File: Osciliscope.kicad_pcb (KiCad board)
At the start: 2 copper layers, 39.6 x 60.2 mm, 42 parts, among them J1 U.FL, J2 Conn_01x04_Socket, J3 U.FL, J4 Conn_01x04_Socket, J5 USB_C_Receptacle_USB2.0_14P, J6 Conn_01x02_MountingPin, SW1 SW_Rotary_1x8_MP, SW2 SW_Rotary_1x8_MP, SW3 SW_Nidec_CAS-120A1, SW4 SW_Nidec_CAS-120A1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

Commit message: pcb update
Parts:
- removed SW1, SW2: SW_Rotary_1x8_MP, Rotary_Encoder:RotaryEncoder_Alps_EC11E-Switch_Vertical_H20mm_CircularMountingHoles
- moved J3 17.6 mm to (80.5, 181.0)
- moved C11 12.9 mm to (104.8, 153.7)
- moved C2 12.9 mm to (77.8, 155.9)
- moved C3 12.9 mm to (108.2, 161.4)
- moved C4 12.9 mm to (99.8, 165.3)
- moved C5 12.9 mm to (94.3, 165.3)
- moved D1 12.9 mm to (111.8, 161.4)
- moved D3 12.9 mm to (82.1, 162.6)
- moved D4 12.9 mm to (79.8, 162.6)
- moved D5 12.9 mm to (79.3, 144.3)
- moved J4 12.9 mm to (94.2, 152.6)
- moved J6 12.9 mm to (77.5, 148.3)
- moved R10 12.9 mm to (108.7, 169.4)
- moved R12 12.9 mm to (93.5, 162.9)
- moved R3 12.9 mm to (112.8, 159.3)
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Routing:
- removed copper zone on F.Cu, net GND
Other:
- board size 39.6 x 60.2 mm -> 51 x 102 mm

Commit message: PCB Fixed
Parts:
- removed J1: U.FL, Connector_Coaxial:BNC_Amphenol_031-5539_Vertical
- added C14: 1uF, Capacitor_SMD:C_1206_3216Metric, F.Cu at (104.1, 123.0)
- added C15: 1uF, Capacitor_SMD:C_1206_3216Metric, F.Cu at (104.1, 126.4)
- added C16: 1uF, Capacitor_SMD:C_1206_3216Metric, F.Cu at (104.1, 129.8)
- added C17: 1uF, Capacitor_SMD:C_1206_3216Metric, F.Cu at (104.1, 133.1)
- added C18: 1uF, Capacitor_SMD:C_1206_3216Metric, F.Cu at (104.1, 136.4)
- added C19: 1uF, Capacitor_SMD:C_1206_3216Metric, F.Cu at (104.1, 139.8)
- added J7: U.FL, Connector_Coaxial:BNC_Amphenol_031-5539_Vertical, F.Cu at (110.8, 180.8)
- added R1: 10k, Capacitor_SMD:C_0603_1608Metric, F.Cu at (108.9, 122.6)
- added R15: 10k, Capacitor_SMD:C_0603_1608Metric, F.Cu at (112.9, 127.7)
- added R16: 10k, Capacitor_SMD:C_0603_1608Metric, F.Cu at (112.9, 130.2)
- added R17: 10k, Capacitor_SMD:C_0603_1608Metric, F.Cu at (98.2, 133.1)
- added R18: 1M, Capacitor_SMD:C_0603_1608Metric, F.Cu at (82.2, 171.4)
- added R19: 1M, Capacitor_SMD:C_0603_1608Metric, F.Cu at (111.8, 170.4)
- added R2: 10k, Capacitor_SMD:C_0603_1608Metric, F.Cu at (108.9, 125.1)
- added R20: 100k, Capacitor_SMD:C_0603_1608Metric, F.Cu at (116.2, 170.4)
- added R5: 10k, Capacitor_SMD:C_0603_1608Metric, F.Cu at (108.9, 127.7)
- added R6: 10k, Capacitor_SMD:C_0603_1608Metric, F.Cu at (108.9, 130.2)
- added R7: 10k, Capacitor_SMD:C_0603_1608Metric, F.Cu at (108.9, 132.7)
- added R8: 10k, Capacitor_SMD:C_0603_1608Metric, F.Cu at (112.9, 122.6)
- added R9: 10k, Capacitor_SMD:C_0603_1608Metric, F.Cu at (112.9, 125.1)
- added SW1: RotaryEncoder_Switch, Rotary_Encoder:RotaryEncoder_Alps_EC11E-Switch_Vertical_H20mm, F.Cu at (78.1, 116.5)
- added SW5: RotaryEncoder_Switch, Rotary_Encoder:RotaryEncoder_Alps_EC11E-Switch_Vertical_H20mm, F.Cu at (97.7, 116.2)
- added SW6: RotaryEncoder_Switch, Rotary_Encoder:RotaryEncoder_Alps_EC11E-Switch_Vertical_H20mm, F.Cu at (78.1, 136.2)
- C10, C9: value 1u -> 1uF
- R14: value 1M -> 100k
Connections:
- C10 pad 1: Net-(J3-In) -> Net-(SW4-A)
- C9 pad 1: Net-(J1-In) -> Net-(SW3-A)
- R14 pad 1: Net-(J3-In) -> Net-(SW4-A)
- R3 pad 2: Net-(D1-A) -> unconnected-(R3-Pad2)
- R4 pad 2: Net-(D3-A) -> Net-(SW4-B)
- SW3 pad 2: Net-(D1-A) -> unconnected-(SW3-B-Pad2)
- SW3 pad 3: Net-(J1-In) -> Net-(SW3-A)
- SW4 pad 2: Net-(D3-A) -> Net-(SW4-B)
- SW4 pad 3: Net-(J3-In) -> Net-(SW4-A)
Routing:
- net Net-(SW4-A): track 0.00 -> 20.9 mm
- net Net-(J7-In): track 0.00 -> 10.0 mm
- net Net-(J1-In): track 16.7 -> 6.75 mm
- net Net-(SW3-A): track 0.00 -> 7.24 mm
- net Net-(J3-In): track 17.7 -> 10.6 mm
- added copper zone on F.Cu, net GND

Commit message: Changes
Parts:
- removed R10: 1M, Capacitor_SMD:C_0603_1608Metric
- added J1: Conn_01x09_Socket, Connector_PinHeader_2.00mm:PinHeader_1x09_P2.00mm_Vertical, F.Cu at (75.0, 113.8)
- moved C15 24.9 mm to (96.2, 102.8)
- moved R5 23.5 mm to (94.8, 108.8), turned to 90 degrees
- moved C14 19.1 mm to (96.2, 105.6)
- moved R2 19.1 mm to (94.8, 112.2), turned to -90 degrees
- moved C17 18.3 mm to (111.2, 116.2)
- moved R9 18.0 mm to (95.0, 123.8), turned to 90 degrees
- moved R15 16.4 mm to (97.0, 123.8), turned to 90 degrees
- moved R1 16.1 mm to (96.6, 112.2), turned to -90 degrees
- moved R16 16.0 mm to (97.2, 127.4), turned to -90 degrees
- moved R7 14.4 mm to (112.8, 118.8)
- moved C16 13.5 mm to (105.2, 116.2), turned to 180 degrees
- moved R6 12.3 mm to (104.6, 118.7)
- moved SW5 10.3 mm to (107.5, 113.1)
- moved C19 10.1 mm to (96.4, 133.2)
- moved C18 9.65 mm to (96.4, 130.6)
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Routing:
- net V3.3: track 81.5 -> 163.7 mm, vias 4 -> 7
- net H_dt: track 0.00 -> 50.7 mm, vias 0 -> 1
- net H_clk: track 0.00 -> 44.6 mm
- net Trig_dt: track 0.00 -> 42.6 mm
- net V_dt: track 0.00 -> 39.6 mm
- net Trig_clk: track 0.00 -> 38.2 mm, vias 0 -> 1
- net Ch2_vis: track 0.00 -> 33.8 mm
- net V_clk: track 0.00 -> 31.9 mm
- net Net-(R7-Pad2): track 0.00 -> 21.7 mm
- net GND: track 27.7 -> 45.2 mm, vias 12 -> 17
- net Net-(R2-Pad2): track 0.00 -> 17.0 mm, vias 0 -> 2
- net Trig_ch: track 0.00 -> 16.6 mm
- net USBCRAW: track 36.8 -> 51.3 mm
- net Net-(D3-A): track 13.2 -> 1.66 mm
- net Net-(SW4-B): track 0.00 -> 10.9 mm
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
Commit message: DOUBLE POWAH
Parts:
- removed D2, D3, D4: D, Diode_SMD:D_0201_0603Metric
- removed J6: Conn_01x02_MountingPin, Connector_PinHeader_2.00mm:PinHeader_1x02_P2.00mm_Vertical
- removed U3: IP2721, Package_SO:TSSOP-16_4.4x5mm_P0.65mm
- removed U8: MCP4251-104E/ML-ND, Package_SO:TSSOP-14-1EP_4.4x5mm_P0.65mm
- added C20: 20pF, Capacitor_SMD:C_1206_3216Metric, F.Cu at (145.8, 99.6)
- added J8: USB_C_Receptacle_USB2.0_14P, Connector_USB:USB_C_Receptacle_Amphenol_124019772112A, F.Cu at (161.0, 95.3)
- added R10: 10k, Capacitor_SMD:C_0603_1608Metric, F.Cu at (116.0, 96.3)
- added R14: 1M, Capacitor_SMD:C_0603_1608Metric, F.Cu at (116.0, 98.8)
- added R18: 10k, Capacitor_SMD:C_0603_1608Metric, F.Cu at (116.0, 101.3)
- added R19: 1M, Capacitor_SMD:C_0603_1608Metric, F.Cu at (116.0, 103.8)
- added R20: 1M, Capacitor_SMD:C_0603_1608Metric, F.Cu at (116.0, 106.3)
- added R21: 1M, Capacitor_SMD:C_0603_1608Metric, F.Cu at (116.0, 108.8)
- C11: value 1uF -> 100n
- C12: value 10u -> 100n
- D1: value D -> 1N4001; footprint Diode_SMD:D_0201_0603Metric -> Diode_THT:D_DO-41_SOD81_P10.16mm_Horizontal
- R14, R20: value 100k -> 1M
- R18: value 1M -> 10k
- R3, R4: value 5k -> 10k
- U4: value AZ1084-5.0 -> CH340N; footprint Package_TO_SOT_SMD:TO-252-2 -> Package_SO:JEITA_SOIC-8_3.9x4.9mm_P1.27mm
- moved U4 73.9 mm to (152.0, 108.6), turned to -90 degrees
- moved D1 72.6 mm to (152.0, 101.0), turned to 90 degrees
- moved C11 60.9 mm to (146.0, 108.9)
- moved J2 59.6 mm to (138.8, 134.2)
- moved C2 59.6 mm to (119.9, 113.8)
- moved C3 59.6 mm to (150.4, 119.3)
- moved C4 59.6 mm to (141.9, 123.2)
- moved C5 59.6 mm to (136.5, 123.2)
- moved D5 59.6 mm to (121.5, 102.2)
- moved R1 59.6 mm to (138.8, 70.1)
- moved R17 59.6 mm to (137.2, 85.3)
- moved R3 59.6 mm to (154.9, 117.2)
- moved R6 59.6 mm to (146.8, 76.5)
- moved J7 59.6 mm to (152.9, 138.7)
- moved R19 59.6 mm to (153.9, 128.3)
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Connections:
- net C2_G_IN renamed Net-(U7--)
- net C2_G_OUT renamed CHAN_2
- C10 pad 1: Net-(SW4-A) -> Net-(J3-In)
- C11 pad 1: USBCRAW -> 5Vin
- C12 pad 1: USBCRAW -> Net-(U4-V3)
- C9 pad 1: Net-(SW3-A) -> Net-(J7-In)
- D1 pad 1: V3.3 -> 5Vin
- J5 pad A4: USBCRAW -> 5Vin
- J5 pad A6: unconnected-(J5-D+-PadA6) -> Net-(U4-UD+)
- J5 pad A7: unconnected-(J5-D--PadA7) -> Net-(U4-UD-)
- J5 pad A9: USBCRAW -> 5Vin
- J5 pad B4: USBCRAW -> 5Vin
- J5 pad B6: unconnected-(J5-D+-PadB6) -> Net-(U4-UD+)
- J5 pad B7: unconnected-(J5-D--PadB7) -> Net-(U4-UD-)
- J5 pad B9: USBCRAW -> 5Vin
- R14 pad 1: Net-(SW4-A) -> GND
- R14 pad 2: GND -> Net-(J3-In)
- R18 pad 1: Net-(SW4-A) -> CHAN_1
- R18 pad 2: Net-(J3-In) -> Net-(U5--)
- R19 pad 1: Net-(SW3-A) -> Net-(J7-In)
- R19 pad 2: Net-(J7-In) -> Net-(SW3-C)
- R20 pad 1: Net-(SW3-A) -> GND
- R20 pad 2: GND -> Net-(J7-In)
- R3 pad 1: C1_G_IN -> Net-(U5--)
- R3 pad 2: unconnected-(R3-Pad2) -> Net-(SW3-B)
- SW3 pad 2: unconnected-(SW3-B-Pad2) -> Net-(SW3-B)
- SW3 pad 3: Net-(SW3-A) -> Net-(J7-In)
- SW4 pad 3: Net-(SW4-A) -> Net-(J3-In)
- U2 pad 5: C1_G_OUT -> CHAN_1
- U4 pad 1: GND -> Net-(U4-UD+)
- U4 pad 2: 5Vin -> Net-(U4-UD-)
- U4 pad 3: USBCRAW -> GND
- U5 pad 1: C1_G_OUT -> CHAN_1
- U5 pad 4: C1_G_IN -> Net-(U5--)
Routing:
- net V3.3: track 163.7 -> 96.4 mm
- net USBCRAW: track 51.3 -> 0.00 mm
- net 5Vin: track 22.5 -> 47.3 mm
- net C1_G_IN: track 19.2 -> 0.00 mm, vias 2 -> 0
- net C1_G_OUT: track 18.2 -> 0.00 mm, vias 2 -> 0
- net Net-(J5-CC2): track 17.7 -> 0.00 mm, vias 2 -> 0
- net RPI_DIN_DP: track 17.3 -> 0.00 mm, vias 2 -> 0
- net Net-(U5--): track 0.00 -> 15.8 mm, vias 0 -> 2
- net Net-(J5-CC1): track 13.3 -> 0.00 mm
- net RPI_SCLK_DP: track 12.4 -> 0.00 mm, vias 2 -> 0
- net Net-(SW3-A): track 11.4 -> 0.00 mm
- net CHAN_2: track 18.6 -> 7.44 mm, vias 2 -> 0
- net Net-(SW4-A): track 10.9 -> 0.00 mm
- net Net-(D1-A): track 2.52 -> 13.4 mm
- net Net-(J3-In): track 10.6 -> 0.00 mm
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
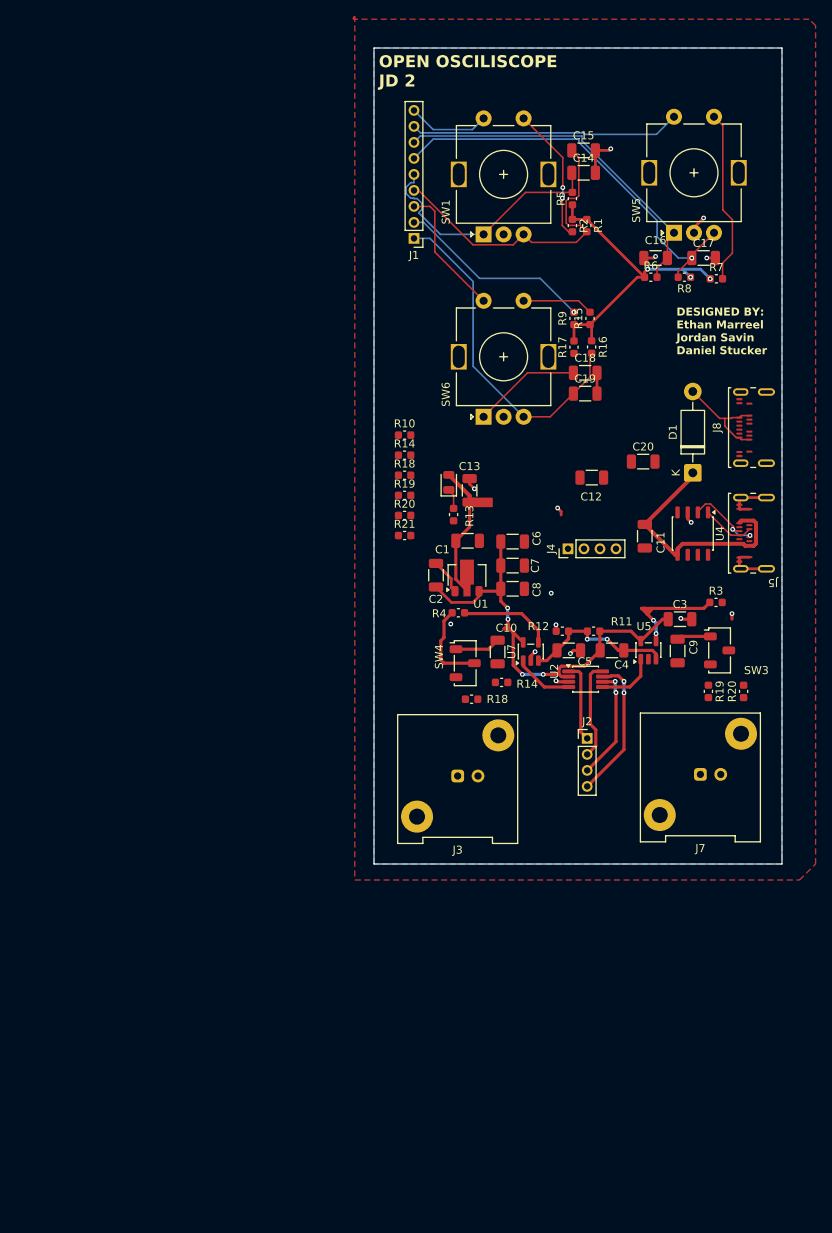
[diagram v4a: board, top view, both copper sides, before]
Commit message: Revert "DOUBLE POWAH"
This reverts commit d7c18ef275ed38aaaeedcd9803d9307ce1c33910.
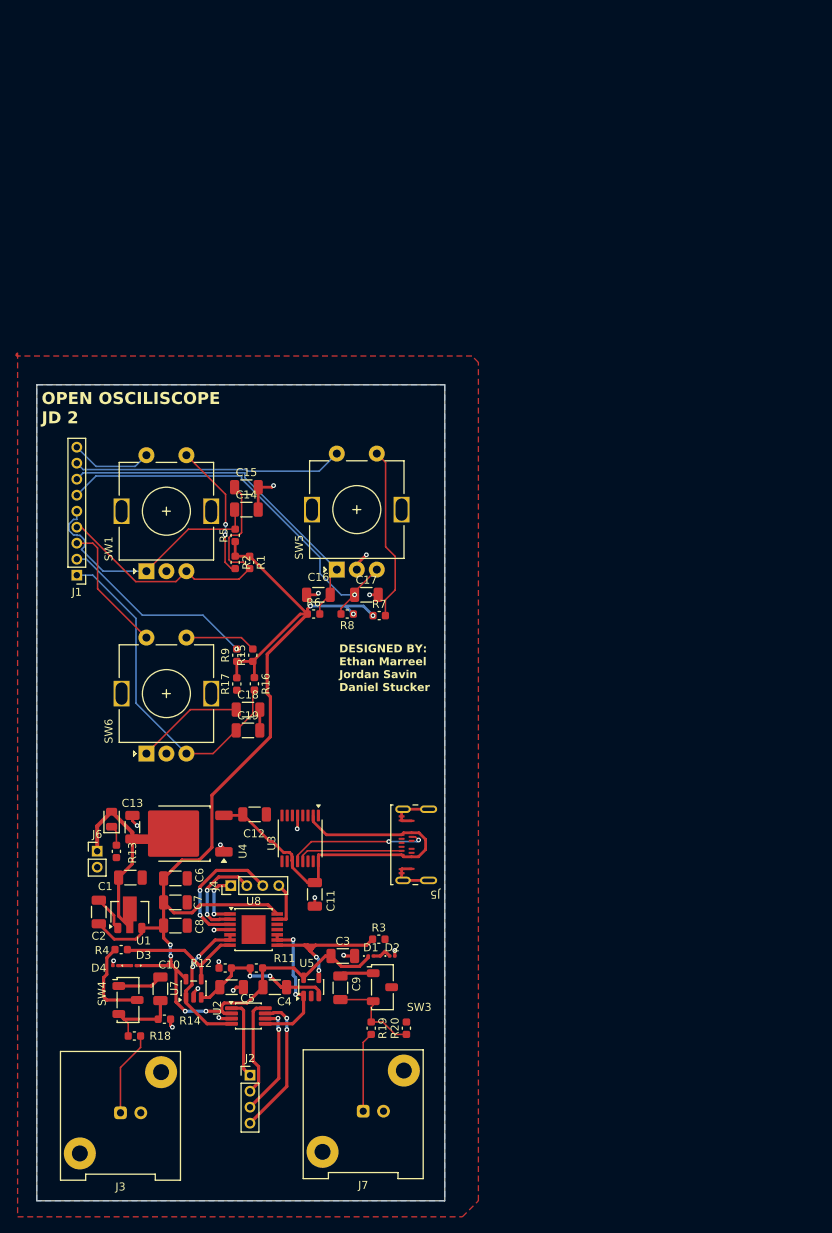
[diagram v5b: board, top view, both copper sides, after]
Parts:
- removed C20: 20pF, Capacitor_SMD:C_1206_3216Metric
- removed J8: USB_C_Receptacle_USB2.0_14P, Connector_USB:USB_C_Receptacle_Amphenol_124019772112A
- removed R10: 10k, Capacitor_SMD:C_0603_1608Metric
- removed the R14 at (116.0, 98.8)
- removed the R18 at (116.0, 101.3)
- removed the R19 at (116.0, 103.8)
- removed the R20 at (116.0, 106.3)
- removed R21: 1M, Capacitor_SMD:C_0603_1608Metric
- added D2: D, Diode_SMD:D_0201_0603Metric, F.Cu at (114.4, 161.4)
- added D3: D, Diode_SMD:D_0201_0603Metric, F.Cu at (82.1, 162.6)
- added D4: D, Diode_SMD:D_0201_0603Metric, F.Cu at (79.8, 162.6)
- added J6: Conn_01x02_MountingPin, Connector_PinHeader_2.00mm:PinHeader_1x02_P2.00mm_Vertical, F.Cu at (77.5, 148.3)
- added U3: IP2721, Package_SO:TSSOP-16_4.4x5mm_P0.65mm, F.Cu at (102.9, 146.7)
- added U8: MCP4251-104E/ML-ND, Package_SO:TSSOP-14-1EP_4.4x5mm_P0.65mm, F.Cu at (97.1, 158.1)
- C11: value 100n -> 1uF
- C12: value 100n -> 10u
- D1: value 1N4001 -> D; footprint Diode_THT:D_DO-41_SOD81_P10.16mm_Horizontal -> Diode_SMD:D_0201_0603Metric
- R14, R20: value 1M -> 100k
- R18: value 10k -> 1M
- R3, R4: value 10k -> 5k
- U4: value CH340N -> AZ1084-5.0; footprint Package_SO:JEITA_SOIC-8_3.9x4.9mm_P1.27mm -> Package_TO_SOT_SMD:TO-252-2
- moved U4 73.9 mm to (88.3, 146.1), turned to 180 degrees
- moved D1 72.6 mm to (111.8, 161.4), turned to 0 degrees
- moved C11 60.9 mm to (104.8, 153.7)
- moved J2 59.6 mm to (96.7, 176.3)
- moved C2 59.6 mm to (77.8, 155.9)
- moved C3 59.6 mm to (108.2, 161.4)
- moved C4 59.6 mm to (99.8, 165.3)
- moved C5 59.6 mm to (94.3, 165.3)
- moved D5 59.6 mm to (79.3, 144.3)
- moved R1 59.6 mm to (96.6, 112.2)
- moved R17 59.6 mm to (95.0, 127.4)
- moved R3 59.6 mm to (112.8, 159.3)
- moved R6 59.6 mm to (104.6, 118.7)
- moved J7 59.6 mm to (110.8, 180.8)
- moved R19 59.6 mm to (111.8, 170.4)
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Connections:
- net CHAN_2 renamed C2_G_OUT
- net Net-(U7--) renamed C2_G_IN
- C10 pad 1: Net-(J3-In) -> Net-(SW4-A)
- C11 pad 1: 5Vin -> USBCRAW
- C12 pad 1: Net-(U4-V3) -> USBCRAW
- C9 pad 1: Net-(J7-In) -> Net-(SW3-A)
- D1 pad 1: 5Vin -> V3.3
- J5 pad A4: 5Vin -> USBCRAW
- J5 pad A6: Net-(U4-UD+) -> unconnected-(J5-D+-PadA6)
- J5 pad A7: Net-(U4-UD-) -> unconnected-(J5-D--PadA7)
- J5 pad A9: 5Vin -> USBCRAW
- J5 pad B4: 5Vin -> USBCRAW
- J5 pad B6: Net-(U4-UD+) -> unconnected-(J5-D+-PadB6)
- J5 pad B7: Net-(U4-UD-) -> unconnected-(J5-D--PadB7)
- J5 pad B9: 5Vin -> USBCRAW
- R14 pad 1: GND -> Net-(SW4-A)
- R14 pad 2: Net-(J3-In) -> GND
- R18 pad 1: CHAN_1 -> Net-(SW4-A)
- R18 pad 2: Net-(U5--) -> Net-(J3-In)
- R19 pad 1: Net-(J7-In) -> Net-(SW3-A)
- R19 pad 2: Net-(SW3-C) -> Net-(J7-In)
- R20 pad 1: GND -> Net-(SW3-A)
- R20 pad 2: Net-(J7-In) -> GND
- R3 pad 1: Net-(U5--) -> C1_G_IN
- R3 pad 2: Net-(SW3-B) -> unconnected-(R3-Pad2)
- SW3 pad 2: Net-(SW3-B) -> unconnected-(SW3-B-Pad2)
- SW3 pad 3: Net-(J7-In) -> Net-(SW3-A)
- SW4 pad 3: Net-(J3-In) -> Net-(SW4-A)
- U2 pad 5: CHAN_1 -> C1_G_OUT
- U4 pad 1: Net-(U4-UD+) -> GND
- U4 pad 2: Net-(U4-UD-) -> 5Vin
- U4 pad 3: GND -> USBCRAW
- U5 pad 1: CHAN_1 -> C1_G_OUT
- U5 pad 4: Net-(U5--) -> C1_G_IN
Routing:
- net V3.3: track 96.4 -> 163.7 mm
- net USBCRAW: track 0.00 -> 51.3 mm
- net 5Vin: track 47.3 -> 22.5 mm
- net C1_G_IN: track 0.00 -> 19.2 mm, vias 0 -> 2
- net C1_G_OUT: track 0.00 -> 18.2 mm, vias 0 -> 2
- net Net-(J5-CC2): track 0.00 -> 17.7 mm, vias 0 -> 2
- net RPI_DIN_DP: track 0.00 -> 17.3 mm, vias 0 -> 2
- net Net-(U5--): track 15.8 -> 0.00 mm, vias 2 -> 0
- net Net-(J5-CC1): track 0.00 -> 13.3 mm
- net RPI_SCLK_DP: track 0.00 -> 12.4 mm, vias 0 -> 2
- net Net-(SW3-A): track 0.00 -> 11.4 mm
- net C2_G_OUT: track 7.44 -> 18.6 mm, vias 0 -> 2
- net Net-(SW4-A): track 0.00 -> 10.9 mm
- net Net-(D1-A): track 13.4 -> 2.52 mm
- net Net-(J3-In): track 0.00 -> 10.6 mm
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
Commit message: DOUBLE POWAH
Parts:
- removed C11: 1uF, Capacitor_SMD:C_1206_3216Metric
- removed C12, C13: 10u, Capacitor_SMD:C_1206_3216Metric
- removed D1, D2, D3, D4: D, Diode_SMD:D_0201_0603Metric
- removed J4: Conn_01x04_Socket, Connector_PinHeader_2.00mm:PinHeader_1x04_P2.00mm_Vertical
- removed SW3: SW_Nidec_CAS-120A1, Button_Switch_SMD:Nidec_Copal_CAS-120A
- removed U4: AZ1084-5.0, Package_TO_SOT_SMD:TO-252-2
- removed U8: MCP4251-104E/ML-ND, Package_SO:TSSOP-14-1EP_4.4x5mm_P0.65mm
- added C20: 20pF, Capacitor_SMD:C_1206_3216Metric, F.Cu at (87.0, 168.4)
- added C21: 20pF, Capacitor_SMD:C_1206_3216Metric, F.Cu at (114.0, 170.8)
- added J8: USB_C_Receptacle_USB2.0_14P, Connector_USB:USB_C_Receptacle_Amphenol_124019772112A, F.Cu at (119.0, 159.9)
- added J9: Conn_01x03_Socket, Connector_PinSocket_2.00mm:PinSocket_1x03_P2.00mm_Vertical, F.Cu at (110.2, 153.6)
- added R10: 5k, Capacitor_SMD:C_0603_1608Metric, F.Cu at (80.6, 159.8)
- added R21: 5.5k, Capacitor_SMD:C_0603_1608Metric, F.Cu at (116.0, 167.0)
- added R22: 5.5k, Capacitor_SMD:C_0603_1608Metric, F.Cu at (111.8, 147.8)
- added R23: 5.5k, Capacitor_SMD:C_0603_1608Metric, F.Cu at (111.8, 144.5)
- added SW7: SW_Nidec_CAS-120A1, Button_Switch_SMD:Nidec_Copal_CAS-120A, F.Cu at (104.2, 166.4)
- added TP1: TestPoint, TestPoint:TestPoint_Pad_3.0x3.0mm, F.Cu at (118.8, 170.8)
- added TP2: TestPoint, TestPoint:TestPoint_Pad_3.0x3.0mm, F.Cu at (77.0, 161.2)
- added TP3: TestPoint, TestPoint:TestPoint_Pad_3.0x3.0mm, F.Cu at (92.0, 168.2)
- added TP4: TestPoint, TestPoint:TestPoint_Pad_3.0x3.0mm, F.Cu at (90.6, 163.2)
- added TP5: TestPoint, TestPoint:TestPoint_Pad_3.0x3.0mm, F.Cu at (77.0, 151.6)
- added TP6: TestPoint, TestPoint:TestPoint_Pad_3.0x3.0mm, F.Cu at (77.0, 156.2)
- added U6: TLV9061xDBV, Package_TO_SOT_SMD:SOT-23-5, F.Cu at (86.2, 151.4)
- J1: footprint Connector_PinHeader_2.00mm:PinHeader_1x09_P2.00mm_Vertical -> Connector_PinSocket_2.00mm:PinSocket_1x09_P2.00mm_Vertical
- J6: footprint Connector_PinHeader_2.00mm:PinHeader_1x02_P2.00mm_Vertical -> Connector_PinSocket_2.00mm:PinSocket_1x02_P2.00mm_Vertical
- R14, R20: value 100k -> 1M
- R18: value 1M -> 5k
- R19: value 1M -> 5.5k
- U3: value IP2721 -> CH340N; footprint Package_SO:TSSOP-16_4.4x5mm_P0.65mm -> Package_SO:JEITA_SOIC-8_3.9x4.9mm_P1.27mm
- moved J6 40.0 mm to (116.6, 139.8), turned to 90 degrees
- moved U1 26.6 mm to (107.4, 149.4), turned to 0 degrees
- moved C1 26.5 mm to (107.0, 143.6)
- moved C2 25.0 mm to (101.8, 149.2)
- moved C4 24.3 mm to (81.0, 149.8), turned to -90 degrees
- moved R18 23.5 mm to (104.0, 162.6), turned to 180 degrees
- moved R13 22.5 mm to (101.2, 141.0), turned to 180 degrees
- moved D5 22.1 mm to (101.4, 144.6), turned to 0 degrees
- moved C5 17.1 mm to (81.0, 154.6), turned to -90 degrees
- moved C8 15.2 mm to (102.5, 158.0), turned to 180 degrees
- moved U3 14.7 mm to (109.2, 160.0), turned to 90 degrees
- moved C3 13.7 mm to (95.9, 155.4), turned to 180 degrees
- moved R11 12.9 mm to (92.0, 151.2)
- moved R12 10.0 mm to (92.0, 153.0), turned to 180 degrees
- moved C6 9.61 mm to (96.6, 149.2), turned to 90 degrees
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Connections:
- net C2_G_IN renamed Net-(U7--)
- net C2_G_OUT renamed CHAN_2
- C4 pad 2: V1.8 -> V1.65RAW
- C5 pad 1: V1.8 -> V1.65RAW
- C9 pad 1: Net-(SW3-A) -> Net-(SW7-A)
- C9 pad 2: Net-(SW3-C) -> Net-(SW7-C)
- J5 pad A4: USBCRAW -> 5Vin
- J5 pad A9: USBCRAW -> 5Vin
- J5 pad B4: USBCRAW -> 5Vin
- J5 pad B9: USBCRAW -> 5Vin
- R11 pad 1: V1.8 -> V1.65RAW
- R12 pad 2: V1.8 -> V1.65RAW
- R14 pad 1: Net-(SW4-A) -> GND
- R14 pad 2: GND -> Net-(J3-In)
- R18 pad 1: Net-(SW4-A) -> CHAN_1
- R18 pad 2: Net-(J3-In) -> Net-(U5--)
- R19 pad 1: Net-(SW3-A) -> GND
- R19 pad 2: Net-(J7-In) -> Net-(J8-CC1)
- R20 pad 1: Net-(SW3-A) -> GND
- R20 pad 2: GND -> Net-(J7-In)
- R3 pad 1: C1_G_IN -> Net-(U5--)
- R3 pad 2: unconnected-(R3-Pad2) -> Net-(SW7-C)
- R4 pad 2: Net-(SW4-B) -> Net-(SW4-C)
- SW4 pad 2: Net-(SW4-B) -> Net-(J3-In)
- U2 pad 5: C1_G_OUT -> CHAN_1
- U3 pad 1: unconnected-(U3-VBUSG-Pad1) -> Net-(U3-UD+)
- U3 pad 2: USBCRAW -> Net-(U3-UD-)
- U3 pad 3: unconnected-(U3-NC-Pad3) -> GND
- U3 pad 4: unconnected-(U3-NC-Pad4) -> RTS
- U3 pad 5: GND -> 5Vin
- U3 pad 6: unconnected-(U3-NC-Pad6) -> TXD
- U3 pad 7: unconnected-(U3-NC-Pad7) -> RXD
- U5 pad 1: C1_G_OUT -> CHAN_1
- U5 pad 3: V1.8 -> V1.65
- U5 pad 4: C1_G_IN -> Net-(U5--)
- U7 pad 3: V1.8 -> V1.65
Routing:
- net V1.65: track 0.00 -> 52.6 mm, vias 0 -> 4
- net USBCRAW: track 51.3 -> 0.00 mm
- net 5Vin: track 22.5 -> 67.6 mm, vias 0 -> 2
- net CHAN_1: track 0.00 -> 29.0 mm
- net Net-(J7-In): track 10.0 -> 35.9 mm
- net Net-(J3-In): track 10.6 -> 36.1 mm
- net V1.8: track 19.2 -> 0.00 mm, vias 2 -> 0
- net C1_G_IN: track 19.2 -> 0.00 mm, vias 2 -> 0
- net GND: track 45.2 -> 64.3 mm
- net Net-(U3-UD-): track 0.00 -> 18.5 mm, vias 0 -> 2
- net C1_G_OUT: track 18.2 -> 0.00 mm, vias 2 -> 0
- net RPI_DIN_DP: track 17.3 -> 0.00 mm, vias 2 -> 0
- net V1.65RAW: track 0.00 -> 15.1 mm
- net Net-(U5--): track 0.00 -> 14.5 mm, vias 0 -> 2
- net Net-(U3-UD+): track 0.00 -> 13.6 mm
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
